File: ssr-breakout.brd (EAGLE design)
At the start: 19 x 44 mm, 15 parts, among them U1 DS2413P

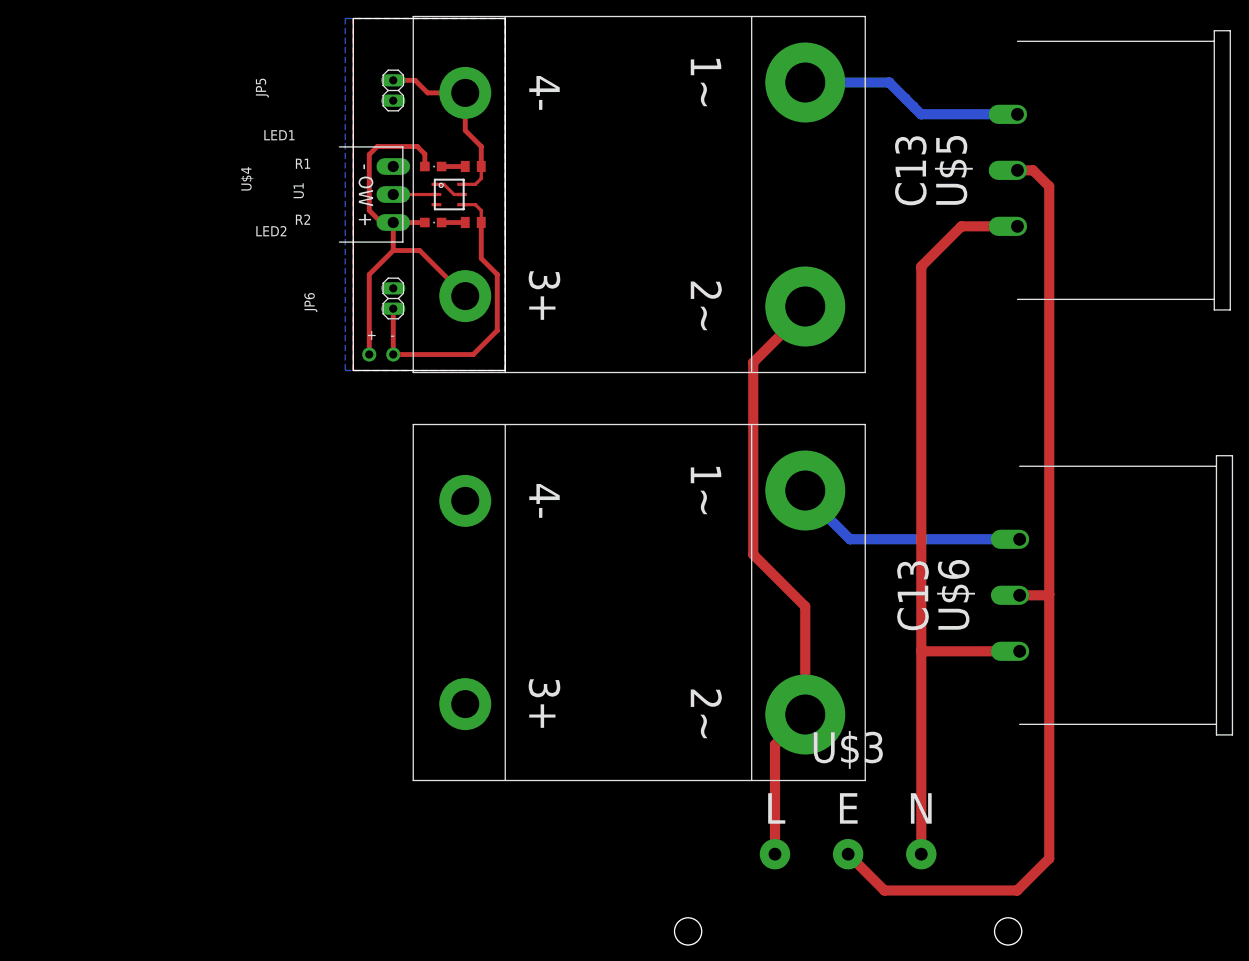
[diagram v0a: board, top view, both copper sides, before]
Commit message: Small updates to layout to fit PQLYT SSR
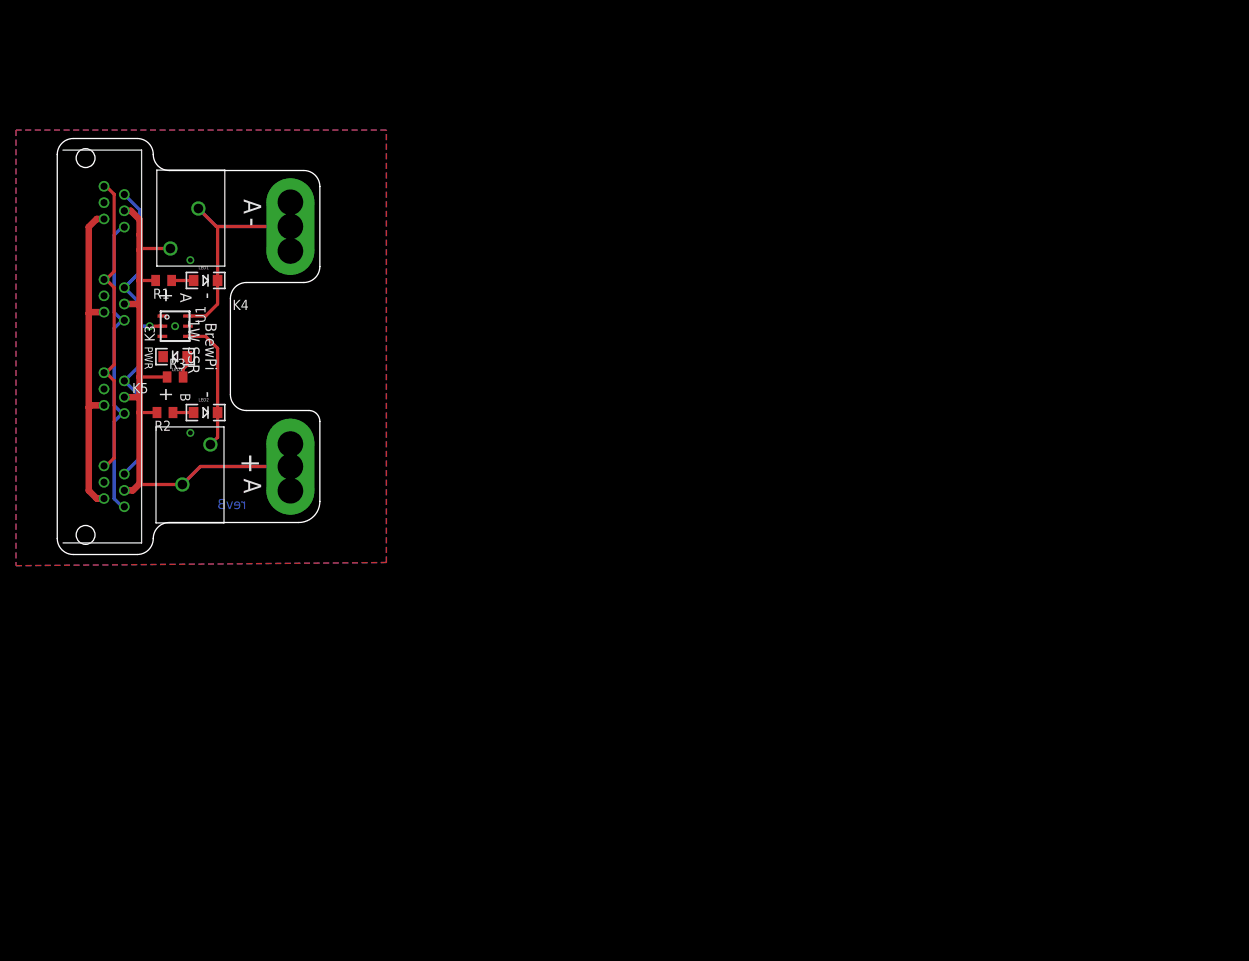
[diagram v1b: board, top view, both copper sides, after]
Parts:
- removed +, -: (no value), adafruit:1X01-CLEANBIG
- removed JP5, JP6: (no value), pinhead:1X02
- removed SSRA, SSRB: PQLYT-XXDA, brewpi:PQLYT
- removed U$3: C14, brewpi:6ESRM-P
- removed U$4: 3.5MM3PHORIZONTAL, elcojacobs:3.5MM3P
- removed U$5, U$6: C13, brewpi:PX0695/10/PC
- added K3: WUERTH_ELEKTRONIK_EICAN_COMMUNICATION_CONNECTORS_6150241439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, brewpi-spark-shield-revA-v04:WUERTH_ELEKTRONIK_EICAN_COMMUNICATION_CONNECTORS_615024143921
- added K4, K5: 691412120002, Wuerth_Elektronik_eiCan_Terminal_Blocks_Connectors:691412120002
- added LED3: GREEN, brewpi-spark-shield-revA-v04:SPARKFUN-LED_LED-1206
- added R3: 470, adafruit:R0805
- added U$1: PQLYT-SINGLESIDE, brewpi:PQLYT-PADS-ONLY
- LED1, LED2: value (none) -> RED; device adafruit:CHIPLED_0805 -> brewpi-spark-shield-revA-v04:SPARKFUN-LED_LED-1206
- moved R2 45.3 mm to (13.5, 17.7)
- moved R1 41.2 mm to (13.3, 34.3)
- moved U1 38.0 mm to (14.7, 28.5)
- moved LED2 37.1 mm to (18.5, 17.7), turned to 0 degrees
- moved LED1 31.8 mm to (18.5, 34.3), turned to 0 degrees
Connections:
- removed net N$10: SSRB.P1, U$6.L
- removed net N$13: U$3.N, U$5.N, U$6.N
- removed net N$6: SSRA.P1, U$5.L
- removed net N$7: SSRA.P2, SSRB.P2, U$3.L
- removed net N$8: U$4.2, U1.2
- removed net N$9: U$3.E, U$5.E, U$6.E
- new net +5V: K3.A3, K3.B3, K3.C3, K3.D3, K4.2, K5.1, R1.2, R2.2, R3.1, U$1.PLUS, U$1.PLUSBOTTOM, U$1.PLUSTOP
- new net 1W: K3.A5, K3.B5, K3.C5, K3.D5, U1.2
- new net RS485-A: K3.A1, K3.B1, K3.C1, K3.D1
- new net RS485-B: K3.A6, K3.B6, K3.C6, K3.D6
- new net VIN: K3.A2, K3.B2, K3.C2, K3.D2
- net GND: now also K3.A4, K3.B4, K3.C4, K3.D4, LED3.C; no longer JP5.2, JP6.2, U$4.1
- net N$1: now also K4.1, LED1.C, U$1.MIN, U$1.MINBOTTOM, U$1.MINTOP; no longer JP5.1, R1.1, SSRA.P4
- net N$2: now also LED1.A, R1.1; no longer LED1.C, R1.2
- net N$3: now also LED2.A, R2.1; no longer LED2.C, R2.2
- net N$4: now also K5.2, LED2.C; no longer -.1, JP6.1, R2.1, SSRB.P4
- net N$5: now also LED3.A, R3.2; no longer +.1, LED1.A, LED2.A, SSRA.P3, SSRB.P3, U$4.3
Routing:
- net N$9: track 121.2 -> 0.00 mm
- net N$13: track 99.9 -> 0.00 mm
- net +5V: track 0.00 -> 87.9 mm
- net N$7: track 75.6 -> 0.00 mm
- net N$5: track 53.0 -> 2.75 mm
- net 1W: track 0.00 -> 42.5 mm, vias 0 -> 1
- net VIN: track 0.00 -> 41.6 mm
- net RS485-B: track 0.00 -> 38.5 mm
- net RS485-A: track 0.00 -> 38.5 mm
- net N$10: track 29.8 -> 0.00 mm
- net N$6: track 28.2 -> 0.00 mm
- net N$4: track 38.5 -> 16.7 mm
- net N$1: track 23.9 -> 37.8 mm
- net N$8: track 5.40 -> 0.00 mm
- net GND: track 3.73 -> 0.00 mm, vias 0 -> 3
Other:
- board size 19 x 44 mm -> 32.8 x 52 mm
- board text added: "+"
- board text added: "-"
- board text added: "1"
- board text added: "1. RS485-A"
- board text added: "2"
- board text added: "2. 12v"
- board text added: "3. 5V"
- board text added: "4. GND"
- board text added: "5"
- board text added: "5. 1-Wire"
- board text added: "6"
- board text added: "6. RS485-B"
- board text added: "A"
- board text added: "A is connected to SSR slots"
- board text added: "B"
- board text added: "BrewPi 1W SSR"
- board text added: "Dual 1-Wire to SSR Outputs: 5V 15mA"
- board text added: "PWR"
- board text added: "revB"
- board text removed: "- OW +"
